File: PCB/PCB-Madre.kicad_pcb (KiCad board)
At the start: 4 copper layers, 90 x 100 mm, 80 parts, among them IC100 AP63203WU-7, J100 2604-3102, J200 2171790001, J201 2086-1104, J300 2086-1102, J301 jumper, J302 2086-1104, J303 2086-1104, Q100 CSD19537Q3, Q101 BSS138, SW300 SW_DIP_x05, U100 TPS26631RGE, U200 ESP32-S3-WROOM-1, U201 USBLC6-2SC6, U300 THVD2450VDRCR

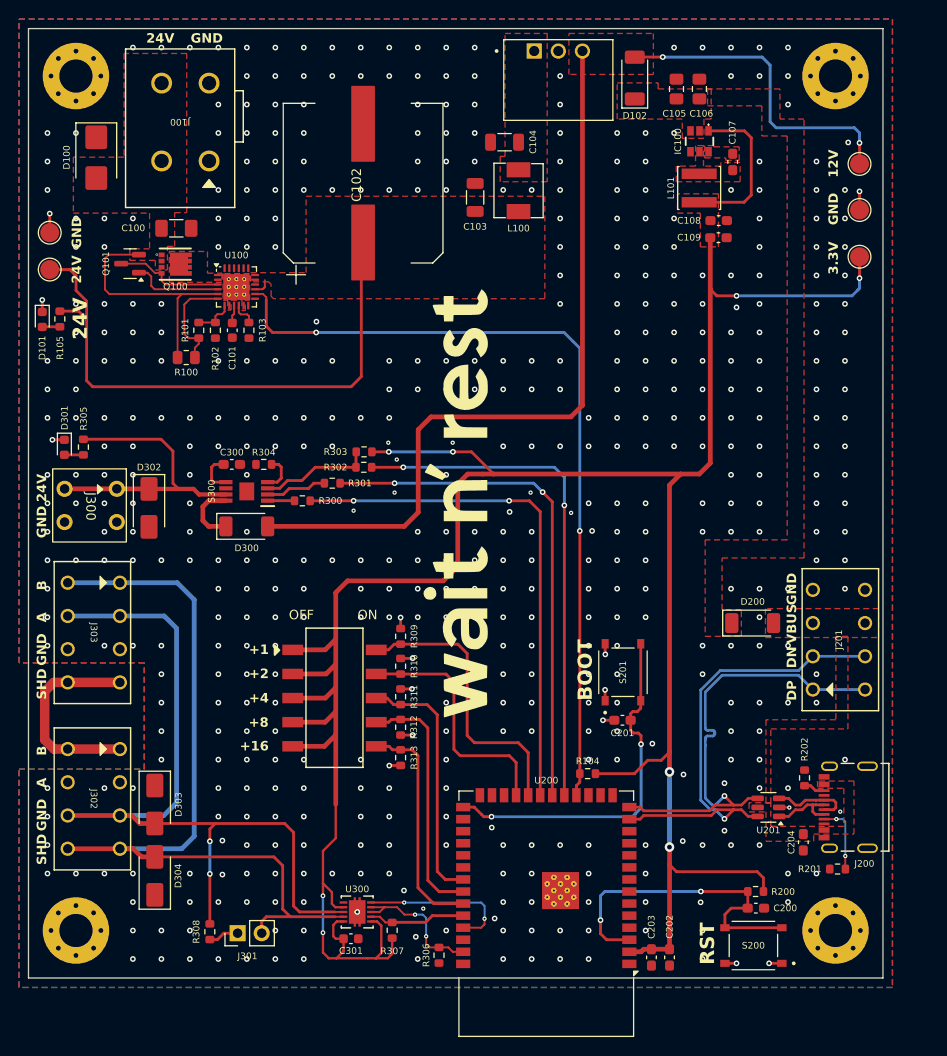
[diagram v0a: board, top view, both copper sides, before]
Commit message: pcb board terminada
Se termino:
- PCB board
- Labels de conectores y logo de la empresa
- Conexion WIZ850IO
- Conexion de MCU y WIZ850IO
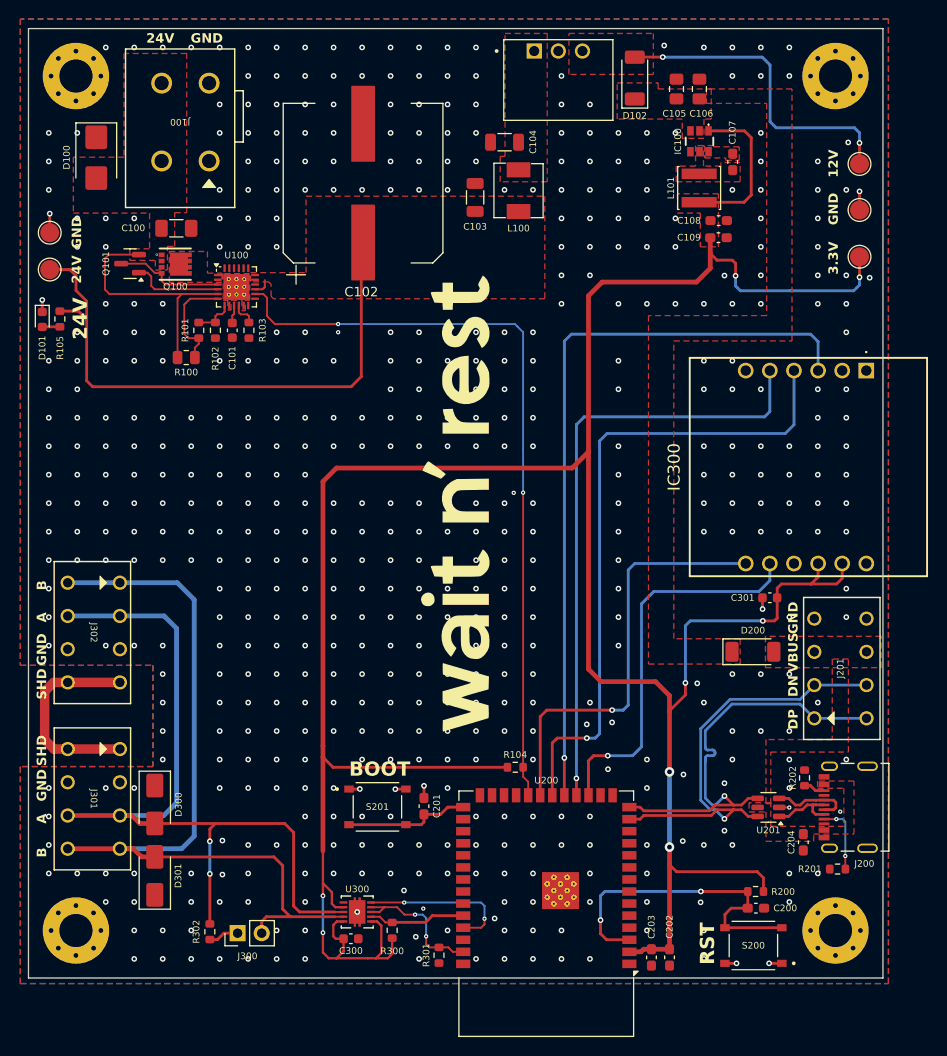
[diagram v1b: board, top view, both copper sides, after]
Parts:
- removed the C300 at (126.4, 93.9)
- removed the D300 at (128.0, 100.4)
- removed the D301 at (108.8, 92.1)
- removed D302: SMAJ15A, Diode_SMD:D_SMA
- removed the J300 at (112.6, 98.3)
- removed the R300 at (133.8, 97.7)
- removed the R301 at (137.0, 95.9)
- removed the R302 at (140.3, 94.2)
- removed R303, R309, R310, R311, R312, R313: 10K, Resistor_SMD:R_0603_1608Metric
- removed R304: 2K, Resistor_SMD:R_0603_1608Metric
- removed R305: 1k, Resistor_SMD:R_0603_1608Metric
- removed S300: TPS1H200AQDGNRQ1, TPS1H200AQDGNRQ1:SOP65P490X110-9N
- removed SW300: SW_DIP_x05, DSIC-05-LS-GER:DSIC-05-LS-GER
- added C301: 0.1uF, Capacitor_SMD:C_0603_1608Metric, F.Cu at (183.1, 108.0)
- added IC300: WIZ850IO, WIZ850IO:WIZ850IO, F.Cu at (193.2, 84.0)
- moved S201 29.5 mm to (141.8, 130.0), turned to 0 degrees
- moved C201 22.8 mm to (146.7, 129.9), turned to 90 degrees
- moved R104 7.65 mm to (156.3, 125.8), turned to 0 degrees
- moved J201 3.04 mm to (187.8, 120.7)
- moved D200 3.02 mm to (181.3, 113.6)
- renumbered C301 to C300, D303 to D300, D304 to D301, J301 to J300, J302 to J301, J303 to J302, R307 to R300, R306 to R301, R308 to R302
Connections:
- net /RS485_EN renamed /MCU/RS485_EN
- U200 pad 17: unconnected-(U200-IO9-Pad17) -> /MCU/RST
- U200 pad 18: /MCU/FLT -> /MCU/CS
- U200 pad 19: /MCU/DOOR_FAULT -> /MCU/MOSI
- U200 pad 20: /MCU/DOOR_DIAG_EN -> /MCU/CLK
- U200 pad 21: /MCU/DOOR_EN -> /MCU/MISO
- U200 pad 22: /ID1 -> /MCU/FLT
- U200 pad 23: /ID2 -> unconnected-(U200-IO21-Pad23)
- U200 pad 33: /ID3 -> unconnected-(U200-IO40-Pad33)
- U200 pad 34: /ID4 -> unconnected-(U200-IO41-Pad34)
- U200 pad 35: /ID5 -> unconnected-(U200-IO42-Pad35)
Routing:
- net +12V: track 114.6 -> 33.8 mm
- net /MCU/MOSI: track 0.00 -> 78.2 mm, vias 0 -> 1
- net /MCU/CLK: track 0.00 -> 68.6 mm, vias 0 -> 1
- net /MCU/CS: track 0.00 -> 64.3 mm, vias 0 -> 1
- net /MCU/DOOR_EN: track 54.6 -> 0.00 mm, vias 2 -> 0
- net /MCU/DOOR_FAULT: track 54.2 -> 0.00 mm, vias 2 -> 0
- net /MCU/DOOR_DIAG_EN: track 54.1 -> 0.00 mm, vias 2 -> 0
- net /MCU/MISO: track 0.00 -> 44.9 mm, vias 0 -> 1
- net /MCU/RST: track 0.00 -> 41.2 mm, vias 0 -> 1
- net Net-(D302-A1): track 31.4 -> 0.00 mm
- net /ID1: track 30.5 -> 0.00 mm
- net /ID3: track 26.7 -> 0.00 mm
- net /ID2: track 26.2 -> 0.00 mm
- net /ID4: track 26.2 -> 0.00 mm
- net /MCU/BOOT: track 38.3 -> 13.3 mm, vias 2 -> 0
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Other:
- board text removed: "+1"
- board text removed: "+16"
- board text removed: "+2"
- board text removed: "+4"
- board text removed: "+8"

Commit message: Mejora de ruteo
- Se ha mejorado el ruteo del sector de potencia
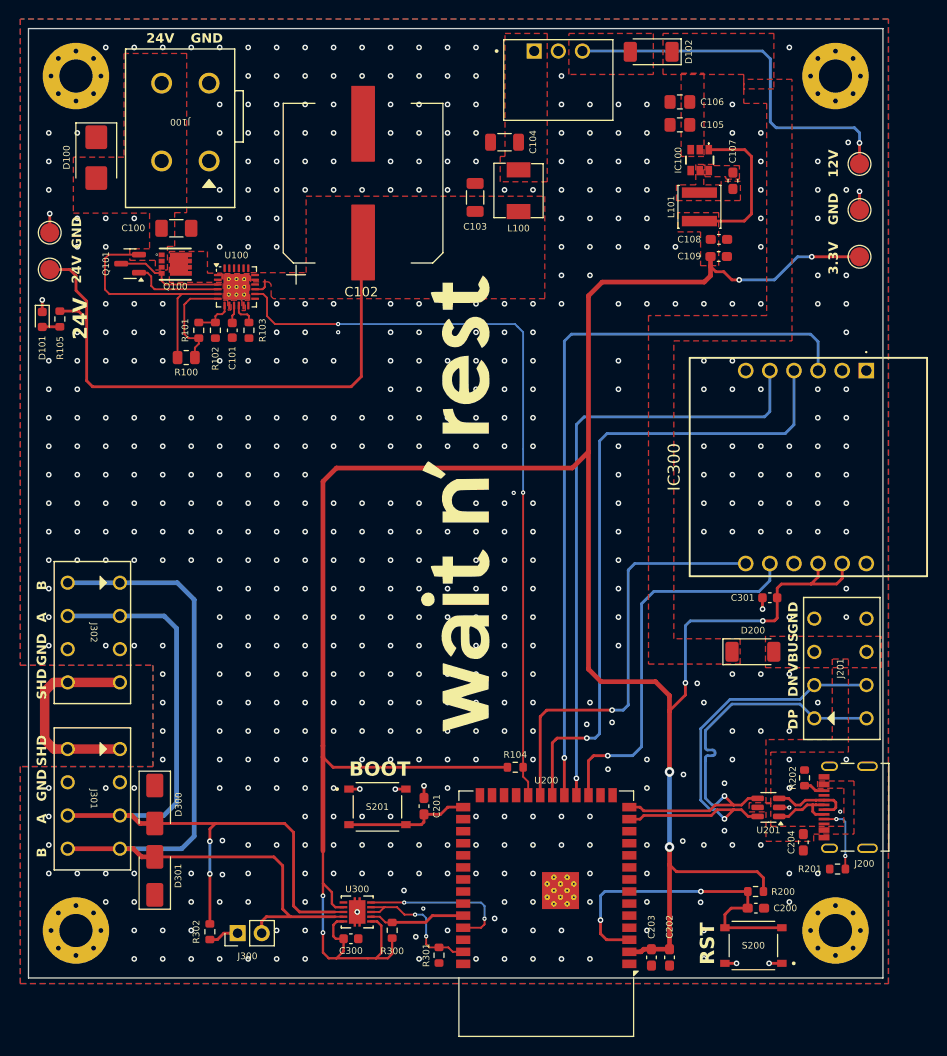
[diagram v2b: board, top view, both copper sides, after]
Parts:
- moved C105 3.79 mm to (173.6, 58.1), turned to 180 degrees
- moved D102 3.26 mm to (170.6, 50.4), turned to 180 degrees
- moved C106 2.47 mm to (173.6, 55.7), turned to 180 degrees
- moved C107 1.98 mm to (179.2, 64.0)
- moved IC100 1.98 mm to (175.7, 61.9)
- moved C108 1.98 mm to (177.7, 70.2)
- moved C109 1.98 mm to (177.7, 72.0)
- moved L101 1.98 mm to (175.7, 66.8)
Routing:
- net +12V: track 33.8 -> 39.9 mm, vias 2 -> 1
- net +3.3V: track 304.9 -> 298.7 mm

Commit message: Cambio del footprint Efuse
- Se ha cambiado el footorint de chip Efuse debido a que el utilizado no habia stock en JLCPCB
- Se ha creado los archivos de configuracion para JLCPCB
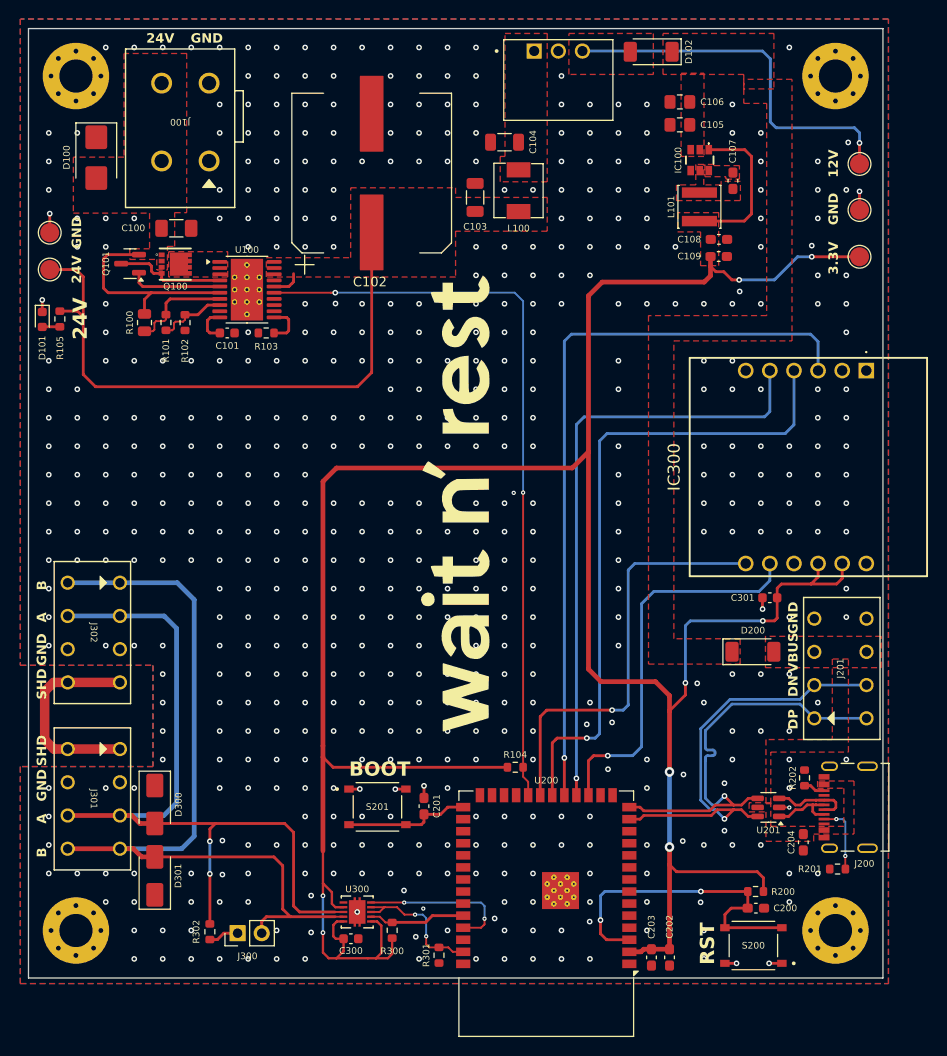
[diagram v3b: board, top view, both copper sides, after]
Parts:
- U100: value TPS26631RGE -> TPS26631PWP; footprint Package_DFN_QFN:Texas_RGE0024H_VQFN-24-1EP_4x4mm_P0.5mm_EP2.7x2.7mm_ThermalVias -> Package_SO:HTSSOP-20-1EP_4.4x6.5mm_P0.65mm_EP3.4x6.5mm_Mask2.96x2.96mm_ThermalVias
- moved R100 5.73 mm to (117.2, 79.0), turned to -90 degrees
- moved R101 3.55 mm to (119.5, 79.0), turned to -90 degrees
- moved R102 3.30 mm to (121.5, 79.0)
- moved R103 1.84 mm to (130.0, 80.1), turned to 180 degrees
- moved C102 1.39 mm to (141.0, 63.4)
- moved U100 1.14 mm to (128.0, 75.5)
- moved C101 0.60 mm to (125.9, 80.1), turned to 180 degrees
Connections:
- U100 pad 10: Net-(U100-ILIM) -> Net-(U100-dVdT)
- U100 pad 11: GND -> Net-(U100-ILIM)
- U100 pad 12: unconnected-(U100-~{SHDN}-Pad12) -> GND
- U100 pad 14: /MCU/FLT -> unconnected-(U100-IMON-Pad14)
- U100 pad 15: +24V -> /MCU/FLT
- U100 pad 16: unconnected-(U100-PGOOD-Pad16) -> +24V
- U100 pad 17: +24V -> unconnected-(U100-PGOOD-Pad17)
- U100 pad 19: unconnected-(U100-NC-Pad19) -> +24V
- U100 pad 20: unconnected-(U100-NC-Pad20) -> +24V
- U100 pad 21: unconnected-(U100-NC-Pad21) -> GND
- U100 pad 3: Net-(Q100-G) -> Net-(Q100-D)
- U100 pad 4: Net-(Q101-G) -> Net-(Q100-G)
- U100 pad 5: /POWER/INPUT -> Net-(Q101-G)
- U100 pad 6: Net-(U100-UVLO) -> /POWER/INPUT
- U100 pad 7: Net-(U100-OVP) -> Net-(U100-UVLO)
- U100 pad 8: GND -> Net-(U100-OVP)
- U100 pad 9: Net-(U100-dVdT) -> GND
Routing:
- net /POWER/INPUT: track 26.0 -> 22.0 mm
- net Net-(U100-OVP): track 4.24 -> 7.40 mm
- net +24V: track 63.1 -> 66.3 mm
- net Net-(U100-dVdT): track 1.92 -> 3.91 mm
- net Net-(U100-ILIM): track 2.63 -> 4.46 mm
- net /MCU/FLT: track 80.0 -> 78.9 mm
- net GND: vias 550 -> 554

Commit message: Fix Stitching vias y USB trace clearance
* Se eliminaron las vías que se encontraban demasiado cercanas a componentes o a ciertas zonas, lo cual representaba un problema común generado por el uso de *stitching vias*.

* Se definió un *clearance* de 0.8 mm para las pistas USB, con el fin de respetar el cálculo de impedancia bajo una configuración *no coplanar*. Esto se debe a que, al estar la PCB completamente rodeada por GND, el par diferencial USB pasaba a comportarse como coplanar. Solo se considera no coplanar cuando existe una separación mínima de tres veces el ancho de la pista (0.286 mm), es decir, aproximadamente 0.8 mm. Esta condición se implementó mediante el uso de *Custom Rules*.
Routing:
- net GND: track 13.6 -> 3.54 mm, vias 554 -> 529
